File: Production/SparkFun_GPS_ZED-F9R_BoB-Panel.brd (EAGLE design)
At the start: 43.2 x 50.8 mm, 140 parts, among them J1 U.FL, J3 QWIIC_RIGHT_ANGLE, J4 QWIIC_RIGHT_ANGLE, U1 DUAL-OPTO_HCPL-073L, U2 U-BLOX_ZED_F9R, U3 UHS_INVERTER_SCHMITT_TRIGGERS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, U4 UHS_INVERTER_SCHMITT_TRIGGERS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, U5 3.3V

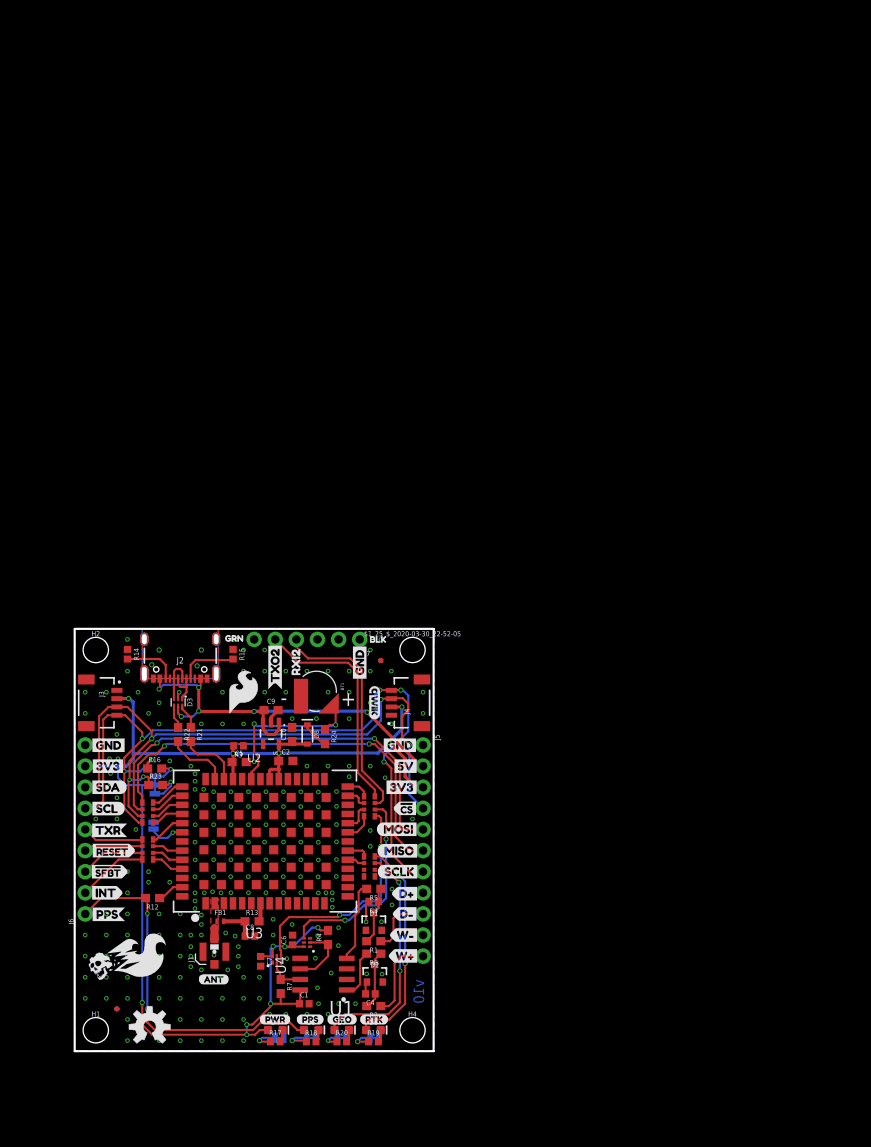
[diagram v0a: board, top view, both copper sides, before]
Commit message: Adds panel to files, deletes buzzard labels
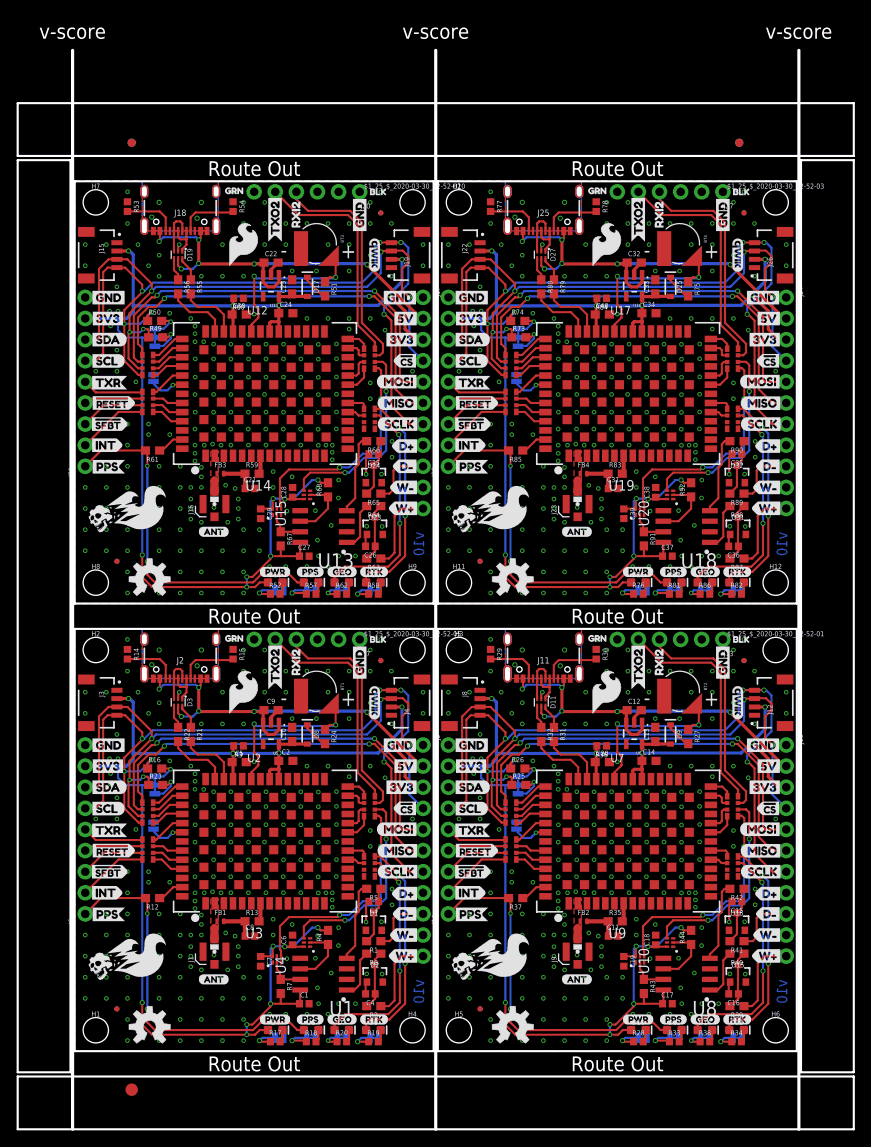
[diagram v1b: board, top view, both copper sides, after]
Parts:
- removed FRAME1: FRAME-LEDGER, SparkFun-Aesthetics:CREATIVE_COMMONS
- added $1_25_$_2020-03-30_22-52-01, $1_25_$_2020-03-30_22-52-02, $1_25_$_2020-03-30_22-52-03, H10, H11, H12, H3, H5, H6, H7, H8, H9: STAND-OFFTIGHT, SparkFun-Hardware:STAND-OFF-TIGHT
- added BT2, BT3, BT4: ML414H_IV01E_BATTERY, SparkFun-Batteries:ML414H_IV01E
- added C11, C21, C31: 47pF, SparkFun-Capacitors:0402
- added C12, C13, C14, C20, C22, C23, C24, C30, C32, C33, C34, C40: 1.0uF, SparkFun-Capacitors:0603
- added C15, C16, C25, C26, C35, C36: 1nF, SparkFun-Capacitors:0402
- added C17, C18, C19, C27, C28, C29, C37, C38, C39: 0.1uF, SparkFun-Capacitors:0402
- added D10, D18, D26: RED, SparkFun-LED:LED-0603
- added D11, D19, D27: PRTR5V0U2F, SparkFun-IC-Power:SOT886
- added D12, D13, D14, D20, D21, D22, D28, D29, D30: BLUE, SparkFun-LED:LED-0603
- added D15, D16, D23, D24, D31, D32: 15V, SparkFun-DiscreteSemi:SOT23-3
- added D17, D25, D9: 0.5A/40V/420mV, SparkFun-DiscreteSemi:SOD-323
- added E$1, E$2, E$3, E$4: (no value), SparkFun-Aesthetics:FIDUCIAL-1X2
- added E$5: (no value), SparkFun-Retired:FIDUCIAL-1.5X3
- added FB2, FB3, FB4: 120NH, SparkFun-Coils:0402_MURATA
- added FD10, FD11, FD12, FD13, FD14, FD15, FD16, FD5, FD6, FD7, FD8, FD9: FIDUCIALUFIDUCIAL, SparkFun-Aesthetics:FIDUCIAL-MICRO
- added J10, J17, J24: (no value), SparkFun-Connectors:1X11_NO_SILK
- added J11, J18, J25: (no value), SparkFun-Connectors:USB-C-16P-2LAYER-PADS
- added J12, J15, J19, J22, J26, J8: QWIIC_RIGHT_ANGLE, SparkFun-Connectors:JST04_1MM_RA
- added J13, J20, J27: (no value), SparkFun-Connectors:1X06_NO_SILK
- added J14, J21, J28: (no value), SparkFun-Connectors:1X09_NO_SILK
- added J16, J23, J9: U.FL, SparkFun-Connectors:U.FL
- added JP10, JP11, JP12, JP15, JP16, JP17, JP18, JP21, JP22, JP23, JP24, JP9: JUMPER-SMT_2_NC_TRACE_SILK, SparkFun-Jumpers:SMT-JUMPER_2_NC_TRACE_SILK
- added JP13, JP19, JP7: JUMPER-SMT_3_2-NC_TRACE_SILK, SparkFun-Jumpers:SMT-JUMPER_3_2-NC_TRACE_SILK
- added JP14, JP20, JP8: JUMPER-SMT_2_NO_SILK, SparkFun-Jumpers:SMT-JUMPER_2_NO_SILK
- added LOGO10, LOGO4, LOGO7: SFE_LOGO_NAME_FLAME.2_INCH, SparkFun-Aesthetics:SFE_LOGO_NAME_FLAME_.2
- added LOGO11, LOGO5, LOGO8: QWIIC_LOGO_4MM, SparkFun-Aesthetics:QWIIC_4MM
- added LOGO12, LOGO6, LOGO9: OSHW-LOGOM, SparkFun-Aesthetics:OSHW-LOGO-M
- added R25, R26, R49, R50, R73, R74: 2.2k, SparkFun-Resistors:0603
- added R27, R39, R41, R51, R63, R65, R75, R87, R89: 3.3k, SparkFun-Resistors:0603
- added R28, R33, R34, R38, R52, R57, R58, R62, R76, R81, R82, R86: 1KOHM-0402-1/16W-1%, SparkFun-Resistors:0402
- added R29, R30, R53, R54, R77, R78: 5.1k, SparkFun-Resistors:0402
- added R31, R32, R55, R56, R79, R80: 27, SparkFun-Resistors:0603
- added R35, R37, R59, R61, R83, R85: 33, SparkFun-Resistors:0603
- added R36, R60, R84: 100K, SparkFun-Resistors:0402
- added R40, R42, R64, R66, R88, R90: 470, SparkFun-Resistors:0603
- added R43, R44, R67, R68, R91, R92: 910, SparkFun-Resistors:0603
- added R45, R46, R47, R48, R69, R70, R71, R72, R93, R94, R95, R96: 33, SparkFun-Resistors:1206_RA
- added U$100, U$166, U$232: (no value), corrected_safe_reset:#RESET2
- added U$101, U$167, U$233: (no value), corrected_safe_reset:#SAFEBOOT3
- added U$102, U$168, U$234: (no value), wat-for-reals:#SFBT0
- added U$103, U$104, U$169, U$170, U$235, U$236: (no value), wat-for-reals:GEO1
- added U$105, U$118, U$171, U$184, U$237, U$250: (no value), wt_dir:D#0
- added U$106, U$119, U$172, U$185, U$238, U$251: (no value), wt_dir:D#1
- added U$107, U$120, U$173, U$186, U$239, U$252: (no value), wt_dir:W#2
- added U$108, U$121, U$174, U$187, U$240, U$253: (no value), wt_dir:W#3
- added U$109, U$175, U$241: (no value), SparkFun-Aesthetics:SFE_LOGO_FLAME_.2
- added U$110, U$176, U$242: (no value), Labels:SCL-[)
- added U$111, U$177, U$243: (no value), Labels:SDA-[)
- added U$112, U$114, U$139, U$141, U$178, U$180, U$205, U$207, U$244, U$246, U$73, U$75: (no value), Labels:3V3-04
- added U$113, U$115, U$125, U$140, U$142, U$144, U$179, U$181, U$191, U$206, U$208, U$210, U$245, U$247, U$257, U$74, U$76, U$78: (no value), Labels:GND-04
- added U$116, U$182, U$248: (no value), Labels:MISO-(]-04
- added U$117, U$183, U$249: (no value), Labels:MOSI-(]-04
- added U$122, U$143, U$188, U$209, U$254, U$77: (no value), Labels:5V
- added U$123, U$189, U$255: (no value), ALL_LABELS:INT1
- added U$124, U$190, U$256: (no value), ALL_LABELS:PPS4
- added U$126, U$146, U$192, U$212, U$258, U$80: (no value), moar:TXO21
- added U$127, U$193, U$259: (no value), txr_rxi:RXI22
- added U$128, U$194, U$260: (no value), txr_rxi:SCLK1
- added U$129, U$195, U$261: (no value), txr_rxi:TXR0
- added U$130, U$196, U$262: (no value), dead reckoning:GPS_DEAD_RECKONING0
- added U$131, U$197, U$263: (no value), Dead#Reckoning#GPS#board#silk#FINAL#png:DEAD#RECKONING#GPS#BOARD#SILK#FINAL#JPG
- added U$132, U$198, U$264: (no value), Dead#Reckoning#GPS#board#silk#FINALSMALL:DEAD#RECKONING#GPS#BOARD#SILK#FINAL#JPG
- added U$133, U$199, U$32: (no value), Labels:CS#-<]-04
- added U$134, U$150, U$200, U$216, U$50, U$84: (no value), ALL labels:PPS8
- added U$135, U$151, U$201, U$217, U$52, U$85: (no value), ALL labels:PWR10
- added U$136, U$149, U$202, U$215, U$57, U$83: (no value), ALL labels:RTK9
- added U$137, U$155, U$203, U$221, U$63, U$89: (no value), TXR:BLK2
- added U$138, U$154, U$204, U$220, U$72, U$88: (no value), TXR:GRN1
- added U$145, U$211, U$79: (no value), ALL_LABELS:RXI28
- added U$147, U$213, U$81: (no value), more_all_labels:SPI4
- added U$148, U$214, U$82: (no value), Labels:I_SUPER2_C-()-04
- added U$152, U$218, U$86: (no value), ant:ANT0
- added U$153, U$219, U$87: (no value), zed:ZED#F9R0
- added U$156, U$222, U$90: (no value), bottom labels:INT2
- added U$157, U$223, U$91: (no value), bottom labels:PPS1
- added U$158, U$224, U$92: (no value), Labels:CS#-[>-04
- added U$159, U$225, U$93: (no value), corrected_bottom:RXI#MOSI0
- added U$160, U$226, U$94: (no value), corrected_bottom:TXO#MISO1
- added U$161, U$227, U$95: (no value), corrected_bottom:SCL#CLK2
- added U$162, U$228, U$96: (no value), corrected_bottom:SCL5
- added U$163, U$229, U$97: (no value), corrected_bottom:SDA4
- added U$164, U$230, U$98: (no value), corrected_bottom:TXR3
- added U$165, U$231, U$99: (no value), corrected_safe_reset:#RESET1
- added U10, U14, U15, U19, U20, U9: UHS_INVERTER_SCHMITT_TRIGGERSIP6, SparkFun-IC-Amplifiers:SIP6
- added U11, U16, U6: 3.3V, SparkFun-IC-Power:SOT23-5
- added U12, U17, U7: U-BLOX_ZED_F9R, SparkFun-GPS:UBLOX_ZED_F9R
- added U13, U18, U8: DUAL-OPTO_HCPL-073L, SparkFun-DiscreteSemi:SOP_8-PIN
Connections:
- new net !RESET1: J14.4, R46.P2
- new net !RESET2: J21.4, R70.P2
- new net !RESET3: J28.4, R94.P2
- new net !SAFEBOOT1: J14.3, R46.P3
- new net !SAFEBOOT2: J21.3, R70.P3
- new net !SAFEBOOT3: J28.3, R94.P3
- new net 3.3V1: C13.1, C14.1, C17.1, C18.1, C19.1, C20.1, D10.A, D9.A, J10.3, J12.2, J14.8, J8.2, JP7.2, R36.2, R43.2, R44.2, U10.P6, U6.5, U7.P33, U7.P34, U7.P38, U8.P8, U9.P6
- new net 3.3V2: C23.1, C24.1, C27.1, C28.1, C29.1, C30.1, D17.A, D18.A, J15.2, J17.3, J19.2, J21.8, JP13.2, R60.2, R67.2, R68.2, U11.5, U12.P33, U12.P34, U12.P38, U13.P8, U14.P6, U15.P6
- new net 3.3V3: C33.1, C34.1, C37.1, C38.1, C39.1, C40.1, D25.A, D26.A, J22.2, J24.3, J26.2, J28.8, JP19.2, R84.2, R91.2, R92.2, U16.5, U17.P33, U17.P34, U17.P38, U18.P8, U19.P6, U20.P6
- new net DIR+1: J10.9, R41.1
- new net DIR+2: J17.9, R65.1
- new net DIR+3: J24.9, R89.1
- new net DIR_IN1: R42.2, U8.P4
- new net DIR_IN2: R66.2, U13.P4
- new net DIR_IN3: R90.2, U18.P4
- new net DIR_OUT1: R47.P6, U10.P4
- new net DIR_OUT2: R71.P6, U15.P4
- new net DIR_OUT3: R95.P6, U20.P4
- new net DIR_SCHMITT1: R44.1, U10.P2, U8.P6
- new net DIR_SCHMITT2: R68.1, U13.P6, U15.P2
- new net DIR_SCHMITT3: R92.1, U18.P6, U20.P2
- new net DMINUS1: R31.2, U7.P39
- new net DMINUS2: R55.2, U12.P39
- new net DMINUS3: R79.2, U17.P39
- new net DPLUS1: R32.2, U7.P40
- new net DPLUS2: R56.2, U12.P40
- new net DPLUS3: R80.2, U17.P40
- new net D_SEL1: JP8.1, U7.P47
- new net D_SEL2: JP14.1, U12.P47
- new net D_SEL3: JP20.1, U17.P47
- new net GEOF_STAT1: D14.A, R48.P7
- new net GEOF_STAT2: D22.A, R72.P7
- new net GEOF_STAT3: D30.A, R96.P7
- new net GND1: BT2.-, C11.2, C12.2, C13.2, C14.2, C15.2, C16.2, C17.2, C18.2, C19.2, C20.2, D11.2, D15.1, D16.1, J10.1, J10.10, J10.8, J11.GND, J11.GND2, J12.1, J13.1, J14.9, J8.1, J9.1, J9.2, JP10.1, JP11.1, JP12.1, JP8.2, JP9.1, R29.1, R30.1, R36.1, U10.P3, U6.2, U7.G1, U7.G10, U7.G11, U7.G12, U7.G13, U7.G14, U7.G15, U7.G16, U7.G17, U7.G18, U7.G19, U7.G2, U7.G20, U7.G21, U7.G22, U7.G23, U7.G24, U7.G25, U7.G26, U7.G27, U7.G28, U7.G29, U7.G3, U7.G30, U7.G31, U7.G32, U7.G33, U7.G34, U7.G35, U7.G36, U7.G37, U7.G38, U7.G39, U7.G4, U7.G40, U7.G41, U7.G42, U7.G43, U7.G44, U7.G45, U7.G46, U7.G47, U7.G48, U7.G5, U7.G6, U7.G7, U7.G8, U7.G9, U7.P1, U7.P12, U7.P14, U7.P3, U7.P32, U7.P37, U7.P41, U7.P48, U8.P2, U8.P3, U8.P5, U9.P3
- new net GND2: BT3.-, C21.2, C22.2, C23.2, C24.2, C25.2, C26.2, C27.2, C28.2, C29.2, C30.2, D19.2, D23.1, D24.1, J15.1, J16.1, J16.2, J17.1, J17.10, J17.8, J18.GND, J18.GND2, J19.1, J20.1, J21.9, JP14.2, JP15.1, JP16.1, JP17.1, JP18.1, R53.1, R54.1, R60.1, U11.2, U12.G1, U12.G10, U12.G11, U12.G12, U12.G13, U12.G14, U12.G15, U12.G16, U12.G17, U12.G18, U12.G19, U12.G2, U12.G20, U12.G21, U12.G22, U12.G23, U12.G24, U12.G25, U12.G26, U12.G27, U12.G28, U12.G29, U12.G3, U12.G30, U12.G31, U12.G32, U12.G33, U12.G34, U12.G35, U12.G36, U12.G37, U12.G38, U12.G39, U12.G4, U12.G40, U12.G41, U12.G42, U12.G43, U12.G44, U12.G45, U12.G46, U12.G47, U12.G48, U12.G5, U12.G6, U12.G7, U12.G8, U12.G9, U12.P1, U12.P12, U12.P14, U12.P3, U12.P32, U12.P37, U12.P41, U12.P48, U13.P2, U13.P3, U13.P5, U14.P3, U15.P3
- new net GND3: BT4.-, C31.2, C32.2, C33.2, C34.2, C35.2, C36.2, C37.2, C38.2, C39.2, C40.2, D27.2, D31.1, D32.1, J22.1, J23.1, J23.2, J24.1, J24.10, J24.8, J25.GND, J25.GND2, J26.1, J27.1, J28.9, JP20.2, JP21.1, JP22.1, JP23.1, JP24.1, R77.1, R78.1, R84.1, U16.2, U17.G1, U17.G10, U17.G11, U17.G12, U17.G13, U17.G14, U17.G15, U17.G16, U17.G17, U17.G18, U17.G19, U17.G2, U17.G20, U17.G21, U17.G22, U17.G23, U17.G24, U17.G25, U17.G26, U17.G27, U17.G28, U17.G29, U17.G3, U17.G30, U17.G31, U17.G32, U17.G33, U17.G34, U17.G35, U17.G36, U17.G37, U17.G38, U17.G39, U17.G4, U17.G40, U17.G41, U17.G42, U17.G43, U17.G44, U17.G45, U17.G46, U17.G47, U17.G48, U17.G5, U17.G6, U17.G7, U17.G8, U17.G9, U17.P1, U17.P12, U17.P14, U17.P3, U17.P32, U17.P37, U17.P41, U17.P48, U18.P2, U18.P3, U18.P5, U19.P3, U20.P3
- new net INT1: J14.2, R46.P4
- new net INT2: J21.2, R70.P4
- new net INT3: J28.2, R94.P4
- new net N$100: R71.P4, U12.P22
- new net N$101: R71.P3, U12.P23
- new net N$102: JP18.2, R62.1
- new net N$103: D22.C, R62.2
- new net N$104: C26.1, D23.3, R63.2, R64.1
- new net N$105: C25.1, D24.3, R65.2, R66.1
- new net N$106: D25.C, R75.2
- new net N$107: JP19.1, R73.2
- new net N$108: JP19.3, R74.2
- new net N$109: J25.B5, R77.2
- new net N$110: J25.A5, R78.2
- new net N$111: JP22.2, R82.1
- new net N$112: JP23.2, R81.1
- new net N$113: D28.C, R81.2
- new net N$114: D29.C, R82.2
- new net N$115: D26.C, R76.2
- new net N$116: JP21.2, R76.1
- new net N$117: C31.1, FB4.P2, R83.1
- new net N$118: D27.3, J25.A6, J25.B6
- new net N$119: D27.1, J25.A7, J25.B7
- new net N$120: D27.6, R79.1
- new net N$121: D27.4, R80.1
- new net N$122: R94.P7, U17.P49
- new net N$123: R94.P5, U17.P51
- new net N$124: R93.P6, U17.P44
- new net N$125: R93.P5, U17.P45
- new net N$126: R94.P8, U17.P46
- new net N$127: R93.P8, U17.P42
- new net N$128: R93.P7, U17.P43
- new net N$129: R95.P1, U17.P27
- new net N$13: D9.C, R27.2
- new net N$130: R95.P2, U17.P26
- new net N$131: R96.P2, U17.P19
- new net N$132: R96.P1, U17.P20
- new net N$133: R85.1, U17.P53
- new net N$134: R94.P6, U17.P50
- new net N$135: R95.P4, U17.P22
- new net N$136: R95.P3, U17.P23
- new net N$137: JP24.2, R86.1
- new net N$138: D30.C, R86.2
- new net N$139: C36.1, D31.3, R87.2, R88.1
- new net N$140: C35.1, D32.3, R89.2, R90.1
- new net N$36: JP7.1, R25.2
- new net N$38: JP7.3, R26.2
- new net N$39: J11.B5, R29.2
- new net N$40: J11.A5, R30.2
- new net N$41: JP10.2, R34.1
- new net N$42: JP11.2, R33.1
- new net N$43: D12.C, R33.2
- new net N$44: D13.C, R34.2
- new net N$45: D10.C, R28.2
- new net N$46: JP9.2, R28.1
- new net N$47: C11.1, FB2.P2, R35.1
- new net N$48: D11.3, J11.A6, J11.B6
- new net N$49: D11.1, J11.A7, J11.B7
- new net N$50: D11.6, R31.1
- new net N$51: D11.4, R32.1
- new net N$52: R46.P7, U7.P49
- new net N$53: R46.P5, U7.P51
- new net N$54: R45.P6, U7.P44
- new net N$55: R45.P5, U7.P45
- new net N$56: R46.P8, U7.P46
- new net N$57: R45.P8, U7.P42
- new net N$58: R45.P7, U7.P43
- new net N$59: R47.P1, U7.P27
- new net N$60: R47.P2, U7.P26
- new net N$61: R48.P2, U7.P19
- new net N$62: R48.P1, U7.P20
- new net N$63: R37.1, U7.P53
- new net N$64: R46.P6, U7.P50
- new net N$65: R47.P4, U7.P22
- new net N$66: R47.P3, U7.P23
- new net N$67: JP12.2, R38.1
- new net N$68: D14.C, R38.2
- new net N$69: C16.1, D15.3, R39.2, R40.1
- new net N$70: C15.1, D16.3, R41.2, R42.1
- new net N$71: D17.C, R51.2
- new net N$72: JP13.1, R49.2
- new net N$73: JP13.3, R50.2
- new net N$74: J18.B5, R53.2
- new net N$75: J18.A5, R54.2
- new net N$76: JP16.2, R58.1
- new net N$77: JP17.2, R57.1
- new net N$78: D20.C, R57.2
- new net N$79: D21.C, R58.2
- new net N$80: D18.C, R52.2
- new net N$81: JP15.2, R52.1
- new net N$82: C21.1, FB3.P2, R59.1
- new net N$83: D19.3, J18.A6, J18.B6
- new net N$84: D19.1, J18.A7, J18.B7
- new net N$85: D19.6, R55.1
- new net N$86: D19.4, R56.1
- new net N$87: R70.P7, U12.P49
- new net N$88: R70.P5, U12.P51
- new net N$89: R69.P6, U12.P44
- new net N$90: R69.P5, U12.P45
- new net N$91: R70.P8, U12.P46
- new net N$92: R69.P8, U12.P42
- new net N$93: R69.P7, U12.P43
- new net N$94: R71.P1, U12.P27
- new net N$95: R71.P2, U12.P26
- new net N$96: R72.P2, U12.P19
- new net N$97: R72.P1, U12.P20
- new net N$98: R61.1, U12.P53
- new net N$99: R70.P6, U12.P50
- new net PPS1: D12.A, J14.1, R37.2
- new net PPS2: D20.A, J21.1, R61.2
- new net PPS3: D28.A, J28.1, R85.2
- new net RF_IN1: FB2.P1, J9.FEED, U7.P2
- new net RF_IN2: FB3.P1, J16.FEED, U12.P2
- new net RF_IN3: FB4.P1, J23.FEED, U17.P2
- new net RTK_STAT1: D13.A, R48.P8
- new net RTK_STAT2: D21.A, R72.P8
- new net RTK_STAT3: D29.A, R96.P8
- new net RXI/MOSI1: J10.5, R45.P2
- new net RXI/MOSI2: J17.5, R69.P2
- new net RXI/MOSI3: J24.5, R93.P2
- new net RXI1: J13.4, R47.P7
- new net RXI3: J20.4, R71.P7
- new net RXI4: J27.4, R95.P7
- new net SCL/CLK1: J10.7, J12.4, J14.6, J8.4, R26.1, R45.P4
- new net SCL/CLK2: J15.4, J17.7, J19.4, J21.6, R50.1, R69.P4
- new net SCL/CLK3: J22.4, J24.7, J26.4, J28.6, R74.1, R93.P4
- new net SDA/!CS1: J10.4, J12.3, J14.7, J8.3, R25.1, R45.P3
- new net SDA/!CS2: J15.3, J17.4, J19.3, J21.7, R49.1, R69.P3
- new net SDA/!CS3: J22.3, J24.4, J26.3, J28.7, R73.1, R93.P3
- new net SHIELD1: J11.SHLD1, J11.SHLD2, J11.SHLD3, J11.SHLD4
- new net SHIELD2: J18.SHLD1, J18.SHLD2, J18.SHLD3, J18.SHLD4
- new net SHIELD3: J25.SHLD1, J25.SHLD2, J25.SHLD3, J25.SHLD4
- new net TXO/MISO1: J10.6, R45.P1
- new net TXO/MISO2: J17.6, R69.P1
- new net TXO/MISO3: J24.6, R93.P1
- new net TXO1: J13.5, R47.P8
- new net TXO3: J20.5, R71.P8
- new net TXO4: J27.5, R95.P8
- new net TX_READY1: J14.5, R46.P1
- new net TX_READY2: J21.5, R70.P1
- new net TX_READY3: J28.5, R94.P1
- new net VIN1: C12.1, D11.5, J10.2, J11.VBUS1, J11.VBUS2, U6.1, U6.3
- new net VIN2: C22.1, D19.5, J17.2, J18.VBUS1, J18.VBUS2, U11.1, U11.3
- new net VIN3: C32.1, D27.5, J24.2, J25.VBUS1, J25.VBUS2, U16.1, U16.3
- new net V_BATT1: BT2.+, R27.1, U7.P36
- new net V_BATT2: BT3.+, R51.1, U12.P36
- new net V_BATT3: BT4.+, R75.1, U17.P36
- new net V_RF1: R35.2, U7.P7
- new net V_RF2: R59.2, U12.P7
- new net V_RF3: R83.2, U17.P7
- new net WT+1: J10.11, R39.1
- new net WT+2: J17.11, R63.1
- new net WT+3: J24.11, R87.1
- new net WT_IN1: R40.2, U8.P1
- new net WT_IN2: R64.2, U13.P1
- new net WT_IN3: R88.2, U18.P1
- new net WT_OUT1: R47.P5, U9.P4
- new net WT_OUT2: R71.P5, U14.P4
- new net WT_OUT3: R95.P5, U19.P4
- new net WT_SCHMITT1: R43.1, U8.P7, U9.P2
- new net WT_SCHMITT2: R67.1, U13.P7, U14.P2
- new net WT_SCHMITT3: R91.1, U18.P7, U19.P2
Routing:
- net 3.3V3: track 0.00 -> 157.0 mm, vias 0 -> 12
- net 3.3V2: track 0.00 -> 157.0 mm, vias 0 -> 12
- net 3.3V1: track 0.00 -> 157.0 mm, vias 0 -> 12
- net SCL/CLK3: track 0.00 -> 97.9 mm, vias 0 -> 6
- net SCL/CLK2: track 0.00 -> 97.9 mm, vias 0 -> 6
- net SCL/CLK1: track 0.00 -> 97.9 mm, vias 0 -> 6
- net SDA/!CS2: track 0.00 -> 82.3 mm, vias 0 -> 5
- net SDA/!CS1: track 0.00 -> 82.3 mm, vias 0 -> 5
- net SDA/!CS3: track 0.00 -> 82.3 mm, vias 0 -> 5
- net RXI/MOSI1: track 0.00 -> 51.3 mm, vias 0 -> 2
- net RXI/MOSI3: track 0.00 -> 51.3 mm, vias 0 -> 2
- net RXI/MOSI2: track 0.00 -> 51.3 mm, vias 0 -> 2
- net VIN3: track 0.00 -> 50.7 mm, vias 0 -> 6
- net VIN2: track 0.00 -> 50.7 mm, vias 0 -> 6
- net VIN1: track 0.00 -> 50.7 mm, vias 0 -> 6
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- added copper zone on layer 1, net GND1
- added copper zone on layer 16, net GND1
- added copper zone on layer 1, net GND2
- added copper zone on layer 16, net GND2
- added copper zone on layer 1, net GND3
- added copper zone on layer 16, net GND3
- added copper zone on layer 1, net RF_IN1
- added copper zone on layer 1, net RF_IN2
- added copper zone on layer 1, net RF_IN3
- added copper zone on layer 1, net SHIELD1
- added copper zone on layer 16, net SHIELD1
- added copper zone on layer 1, net SHIELD2
- added copper zone on layer 16, net SHIELD2
- added copper zone on layer 1, net SHIELD3
- added copper zone on layer 16, net SHIELD3
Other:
- board size 43.2 x 50.8 mm -> 100.6 x 129.8 mm
- board text added: "Route Out"
- board text added: "v-score"
- board text removed: "Elias Santistevan"
- board text removed: "Units In Inches"

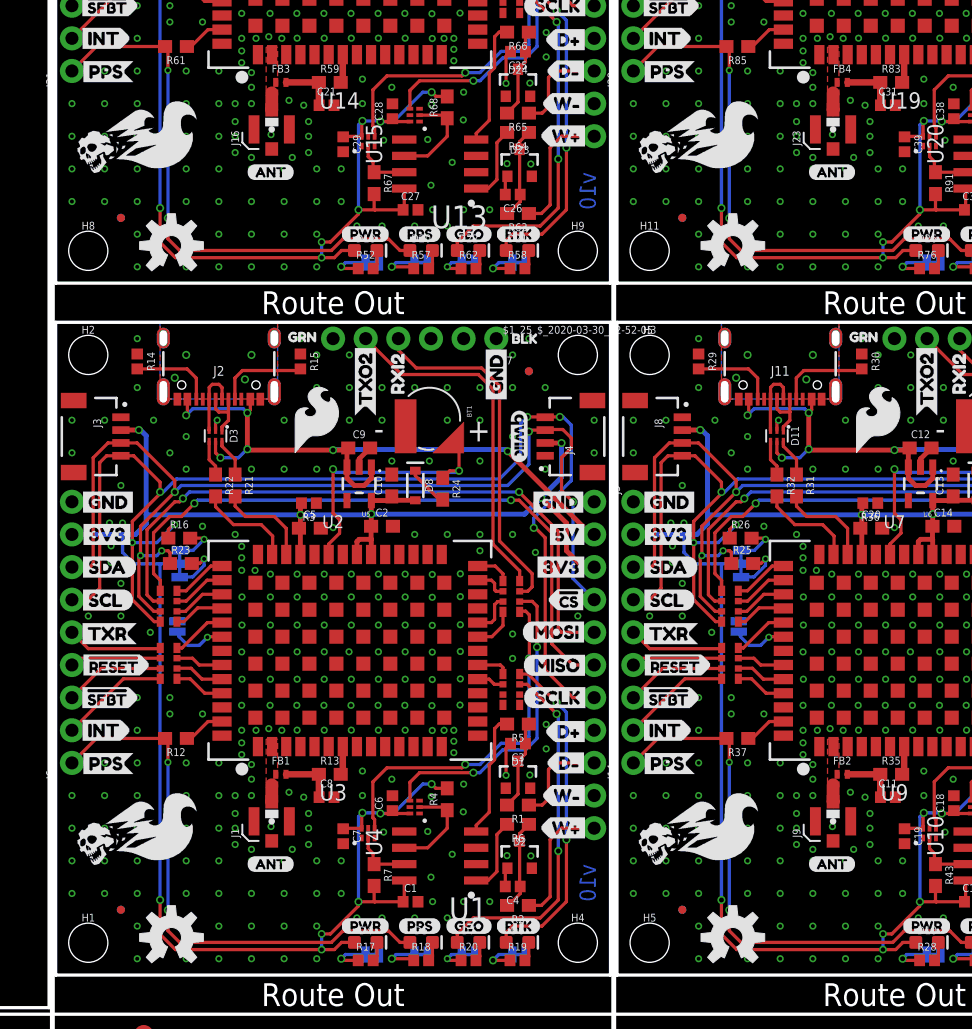
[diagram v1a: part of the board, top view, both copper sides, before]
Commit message: Adds silk for 3 axes and repanelizes
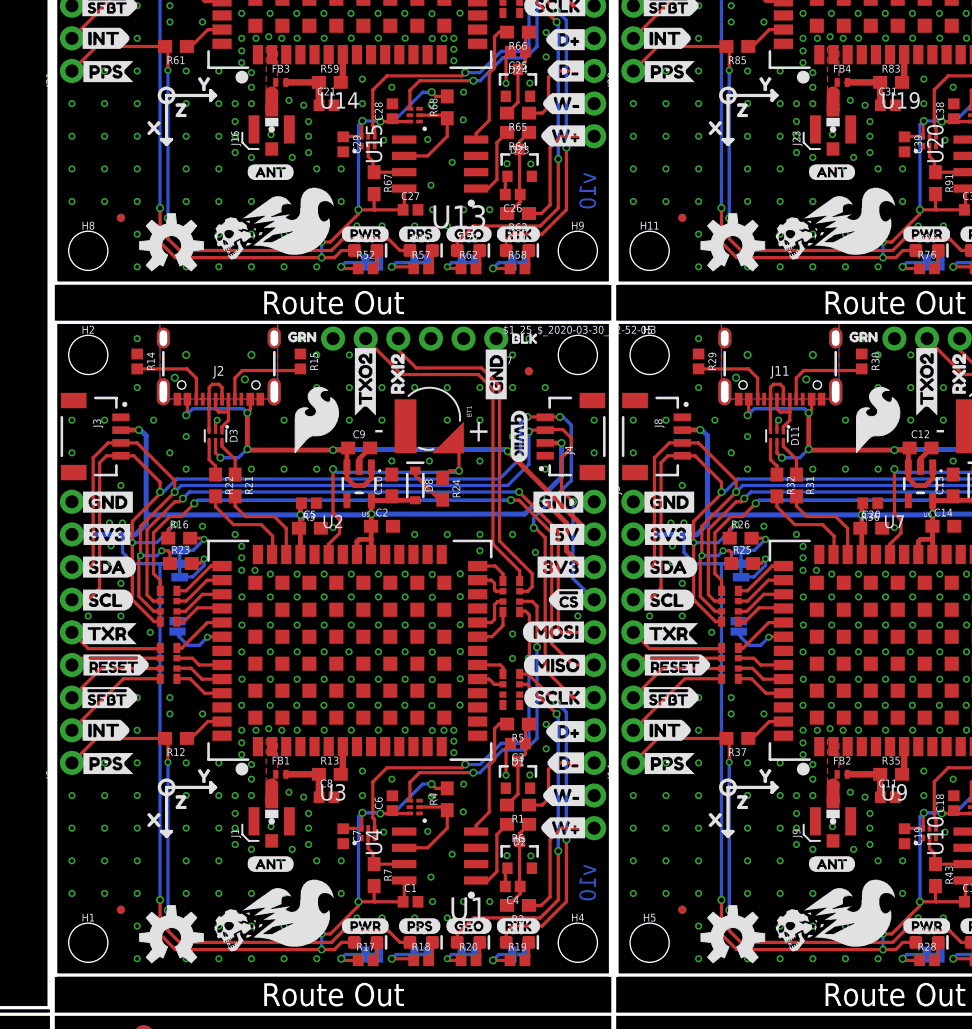
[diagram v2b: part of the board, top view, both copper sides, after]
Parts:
- added U$265: (no value), wt_dir:D#0
- added U$266: (no value), wt_dir:D#1
- added U$267: (no value), wt_dir:W#2
- added U$268: (no value), wt_dir:W#3
- added U$269: (no value), Labels:5V
- added U$270: (no value), ALL_LABELS:INT1
- added U$271: (no value), ALL_LABELS:PPS4
- added U$272: (no value), Labels:GND-04
- added U$273: (no value), moar:TXO21
- added U$274: (no value), txr_rxi:RXI22
- added U$275: (no value), txr_rxi:SCLK1
- added U$276: (no value), txr_rxi:TXR0
- added U$277: (no value), dead reckoning:GPS_DEAD_RECKONING0
- added U$278: (no value), Dead#Reckoning#GPS#board#silk#FINAL#png:DEAD#RECKONING#GPS#BOARD#SILK#FINAL#JPG
- added U$279: (no value), Dead#Reckoning#GPS#board#silk#FINALSMALL:DEAD#RECKONING#GPS#BOARD#SILK#FINAL#JPG
- added U$280: (no value), Orientation:X1
- added U$281, U$282: (no value), Orientation:Y2
- added U$283, U$284: (no value), Orientation:Z0
- U$100: device corrected_safe_reset:#RESET2 -> corrected_bottom:SCL#CLK2
- U$101: device corrected_safe_reset:#SAFEBOOT3 -> corrected_bottom:SCL5
- U$102: device wat-for-reals:#SFBT0 -> corrected_bottom:SDA4
- U$103: device wat-for-reals:GEO1 -> corrected_bottom:TXR3
- U$104: device wat-for-reals:GEO1 -> corrected_safe_reset:#RESET1
- U$105: device wt_dir:D#0 -> corrected_safe_reset:#RESET2
- U$106: device wt_dir:D#1 -> corrected_safe_reset:#SAFEBOOT3
- U$107: device wt_dir:W#2 -> wat-for-reals:#SFBT0
- U$108: device wt_dir:W#3 -> wat-for-reals:GEO1
- U$109: device SparkFun-Aesthetics:SFE_LOGO_FLAME_.2 -> wat-for-reals:GEO1
- U$110: device Labels:SCL-[) -> wt_dir:D#0
- U$111: device Labels:SDA-[) -> wt_dir:D#1
- U$112: device Labels:3V3-04 -> wt_dir:W#2
- U$113: device Labels:GND-04 -> wt_dir:W#3
- U$114: device Labels:3V3-04 -> SparkFun-Aesthetics:SFE_LOGO_FLAME_.2
- U$115, U$257: device Labels:GND-04 -> Labels:SCL-[)
- U$116: device Labels:MISO-(]-04 -> Labels:SDA-[)
- U$117: device Labels:MOSI-(]-04 -> Labels:3V3-04
- U$118: device wt_dir:D#0 -> Labels:GND-04
- U$119: device wt_dir:D#1 -> Labels:3V3-04
- U$120: device wt_dir:W#2 -> Labels:GND-04
- U$121: device wt_dir:W#3 -> Labels:MISO-(]-04
- U$122: device Labels:5V -> Labels:MOSI-(]-04
- U$123: device ALL_LABELS:INT1 -> wt_dir:D#0
- U$124: device ALL_LABELS:PPS4 -> wt_dir:D#1
- U$125: device Labels:GND-04 -> wt_dir:W#2
- U$126: device moar:TXO21 -> wt_dir:W#3
- U$127: device txr_rxi:RXI22 -> Labels:5V
- U$128: device txr_rxi:SCLK1 -> ALL_LABELS:INT1
- U$129: device txr_rxi:TXR0 -> ALL_LABELS:PPS4
- U$130, U$262: device dead reckoning:GPS_DEAD_RECKONING0 -> Labels:GND-04
- U$131: device Dead#Reckoning#GPS#board#silk#FINAL#png:DEAD#RECKONING#GPS#BOARD#SILK#FINAL#JPG -> moar:TXO21
- U$132: device Dead#Reckoning#GPS#board#silk#FINALSMALL:DEAD#RECKONING#GPS#BOARD#SILK#FINAL#JPG -> txr_rxi:RXI22
- U$133: device Labels:CS#-<]-04 -> txr_rxi:SCLK1
- U$134: device ALL labels:PPS8 -> txr_rxi:TXR0
- U$135: device ALL labels:PWR10 -> dead reckoning:GPS_DEAD_RECKONING0
- U$136: device ALL labels:RTK9 -> Dead#Reckoning#GPS#board#silk#FINAL#png:DEAD#RECKONING#GPS#BOARD#SILK#FINAL#JPG
- U$137: device TXR:BLK2 -> Dead#Reckoning#GPS#board#silk#FINALSMALL:DEAD#RECKONING#GPS#BOARD#SILK#FINAL#JPG
- U$138: device TXR:GRN1 -> Orientation:X1
- U$139: device Labels:3V3-04 -> Orientation:Y2
- U$140, U$210: device Labels:GND-04 -> Orientation:Y2
- U$141: device Labels:3V3-04 -> Orientation:Z0
- U$142: device Labels:GND-04 -> Orientation:Z0
- U$143: device Labels:5V -> Labels:CS#-<]-04
- U$144: device Labels:GND-04 -> ALL labels:PPS8
- U$145: device ALL_LABELS:RXI28 -> ALL labels:PWR10
- U$146: device moar:TXO21 -> ALL labels:RTK9
- U$147: device more_all_labels:SPI4 -> TXR:BLK2
- U$148: device Labels:I_SUPER2_C-()-04 -> TXR:GRN1
- U$149: device ALL labels:RTK9 -> Labels:3V3-04
- U$150: device ALL labels:PPS8 -> Labels:GND-04
- U$151: device ALL labels:PWR10 -> Labels:3V3-04
- U$152: device ant:ANT0 -> Labels:GND-04
- U$153: device zed:ZED#F9R0 -> Labels:5V
- U$154: device TXR:GRN1 -> Labels:GND-04
- U$155: device TXR:BLK2 -> ALL_LABELS:RXI28
- U$156: device bottom labels:INT2 -> moar:TXO21
- U$157: device bottom labels:PPS1 -> more_all_labels:SPI4
- U$158: device Labels:CS#-[>-04 -> Labels:I_SUPER2_C-()-04
- U$159: device corrected_bottom:RXI#MOSI0 -> ALL labels:RTK9
- U$160: device corrected_bottom:TXO#MISO1 -> ALL labels:PPS8
- U$161: device corrected_bottom:SCL#CLK2 -> ALL labels:PWR10
- U$162: device corrected_bottom:SCL5 -> ant:ANT0
- U$163: device corrected_bottom:SDA4 -> zed:ZED#F9R0
- U$164: device corrected_bottom:TXR3 -> TXR:GRN1
- U$165: device corrected_safe_reset:#RESET1 -> TXR:BLK2
- U$166: device corrected_safe_reset:#RESET2 -> bottom labels:INT2
- U$167: device corrected_safe_reset:#SAFEBOOT3 -> bottom labels:PPS1
- U$168: device wat-for-reals:#SFBT0 -> Labels:CS#-[>-04
- U$169: device wat-for-reals:GEO1 -> corrected_bottom:RXI#MOSI0
- U$170: device wat-for-reals:GEO1 -> corrected_bottom:TXO#MISO1
- U$171: device wt_dir:D#0 -> corrected_bottom:SCL#CLK2
- U$172: device wt_dir:D#1 -> corrected_bottom:SCL5
- U$173: device wt_dir:W#2 -> corrected_bottom:SDA4
- U$174: device wt_dir:W#3 -> corrected_bottom:TXR3
- U$175: device SparkFun-Aesthetics:SFE_LOGO_FLAME_.2 -> corrected_safe_reset:#RESET1
- U$176: device Labels:SCL-[) -> corrected_safe_reset:#RESET2
- U$177: device Labels:SDA-[) -> corrected_safe_reset:#SAFEBOOT3
- U$178: device Labels:3V3-04 -> wat-for-reals:#SFBT0
- U$179: device Labels:GND-04 -> wat-for-reals:GEO1
- U$180: device Labels:3V3-04 -> wat-for-reals:GEO1
- U$181: device Labels:GND-04 -> wt_dir:D#0
- U$182: device Labels:MISO-(]-04 -> wt_dir:D#1
- U$183: device Labels:MOSI-(]-04 -> wt_dir:W#2
- U$184: device wt_dir:D#0 -> wt_dir:W#3
- U$185: device wt_dir:D#1 -> SparkFun-Aesthetics:SFE_LOGO_FLAME_.2
- U$186: device wt_dir:W#2 -> Labels:SCL-[)
- U$187: device wt_dir:W#3 -> Labels:SDA-[)
- U$188: device Labels:5V -> Labels:3V3-04
- U$189: device ALL_LABELS:INT1 -> Labels:GND-04
- U$190: device ALL_LABELS:PPS4 -> Labels:3V3-04
- U$192: device moar:TXO21 -> Labels:MISO-(]-04
- U$193: device txr_rxi:RXI22 -> Labels:MOSI-(]-04
- U$194: device txr_rxi:SCLK1 -> wt_dir:D#0
- U$195: device txr_rxi:TXR0 -> wt_dir:D#1
- U$196: device dead reckoning:GPS_DEAD_RECKONING0 -> wt_dir:W#2
- U$197: device Dead#Reckoning#GPS#board#silk#FINAL#png:DEAD#RECKONING#GPS#BOARD#SILK#FINAL#JPG -> wt_dir:W#3
- U$198: device Dead#Reckoning#GPS#board#silk#FINALSMALL:DEAD#RECKONING#GPS#BOARD#SILK#FINAL#JPG -> Labels:5V
- U$199: device Labels:CS#-<]-04 -> ALL_LABELS:INT1
- U$200: device ALL labels:PPS8 -> ALL_LABELS:PPS4
- U$201: device ALL labels:PWR10 -> Labels:GND-04
- U$202: device ALL labels:RTK9 -> moar:TXO21
- U$203: device TXR:BLK2 -> txr_rxi:RXI22
- U$204: device TXR:GRN1 -> txr_rxi:SCLK1
- U$205: device Labels:3V3-04 -> txr_rxi:TXR0
- U$206: device Labels:GND-04 -> dead reckoning:GPS_DEAD_RECKONING0
- U$207: device Labels:3V3-04 -> Dead#Reckoning#GPS#board#silk#FINAL#png:DEAD#RECKONING#GPS#BOARD#SILK#FINAL#JPG
- U$208: device Labels:GND-04 -> Dead#Reckoning#GPS#board#silk#FINALSMALL:DEAD#RECKONING#GPS#BOARD#SILK#FINAL#JPG
- U$209: device Labels:5V -> Orientation:X1
- U$211: device ALL_LABELS:RXI28 -> Orientation:Y2
- U$212: device moar:TXO21 -> Orientation:Z0
- U$213: device more_all_labels:SPI4 -> Orientation:Z0
- U$214: device Labels:I_SUPER2_C-()-04 -> Labels:CS#-<]-04
- U$215: device ALL labels:RTK9 -> ALL labels:PPS8
- U$216: device ALL labels:PPS8 -> ALL labels:PWR10
- U$217: device ALL labels:PWR10 -> ALL labels:RTK9
- U$218: device ant:ANT0 -> TXR:BLK2
- U$219: device zed:ZED#F9R0 -> TXR:GRN1
- U$220: device TXR:GRN1 -> Labels:3V3-04
- U$221: device TXR:BLK2 -> Labels:GND-04
- U$222: device bottom labels:INT2 -> Labels:3V3-04
- U$223: device bottom labels:PPS1 -> Labels:GND-04
- U$224: device Labels:CS#-[>-04 -> Labels:5V
- U$225: device corrected_bottom:RXI#MOSI0 -> Labels:GND-04
- U$226: device corrected_bottom:TXO#MISO1 -> ALL_LABELS:RXI28
- U$227: device corrected_bottom:SCL#CLK2 -> moar:TXO21
- U$228: device corrected_bottom:SCL5 -> more_all_labels:SPI4
- U$229: device corrected_bottom:SDA4 -> Labels:I_SUPER2_C-()-04
- U$230: device corrected_bottom:TXR3 -> ALL labels:RTK9
- U$231: device corrected_safe_reset:#RESET1 -> ALL labels:PPS8
- U$232: device corrected_safe_reset:#RESET2 -> ALL labels:PWR10
- U$233: device corrected_safe_reset:#SAFEBOOT3 -> ant:ANT0
- U$234: device wat-for-reals:#SFBT0 -> zed:ZED#F9R0
- U$235: device wat-for-reals:GEO1 -> TXR:GRN1
- U$236: device wat-for-reals:GEO1 -> TXR:BLK2
- U$237: device wt_dir:D#0 -> bottom labels:INT2
- U$238: device wt_dir:D#1 -> bottom labels:PPS1
- U$239: device wt_dir:W#2 -> Labels:CS#-[>-04
- U$240: device wt_dir:W#3 -> corrected_bottom:RXI#MOSI0
- U$241: device SparkFun-Aesthetics:SFE_LOGO_FLAME_.2 -> corrected_bottom:TXO#MISO1
- U$242: device Labels:SCL-[) -> corrected_bottom:SCL#CLK2
- U$243: device Labels:SDA-[) -> corrected_bottom:SCL5
- U$244: device Labels:3V3-04 -> corrected_bottom:SDA4
- U$245: device Labels:GND-04 -> corrected_bottom:TXR3
- U$246: device Labels:3V3-04 -> corrected_safe_reset:#RESET1
- U$247: device Labels:GND-04 -> corrected_safe_reset:#RESET2
- U$248: device Labels:MISO-(]-04 -> corrected_safe_reset:#SAFEBOOT3
- U$249: device Labels:MOSI-(]-04 -> wat-for-reals:#SFBT0
- U$250: device wt_dir:D#0 -> wat-for-reals:GEO1
- U$251: device wt_dir:D#1 -> wat-for-reals:GEO1
- U$252: device wt_dir:W#2 -> wt_dir:D#0
- U$253: device wt_dir:W#3 -> wt_dir:D#1
- U$254: device Labels:5V -> wt_dir:W#2
- U$255: device ALL_LABELS:INT1 -> wt_dir:W#3
- U$256: device ALL_LABELS:PPS4 -> SparkFun-Aesthetics:SFE_LOGO_FLAME_.2
- U$258: device moar:TXO21 -> Labels:SDA-[)
- U$259: device txr_rxi:RXI22 -> Labels:3V3-04
- U$260: device txr_rxi:SCLK1 -> Labels:GND-04
- U$261: device txr_rxi:TXR0 -> Labels:3V3-04
- U$263: device Dead#Reckoning#GPS#board#silk#FINAL#png:DEAD#RECKONING#GPS#BOARD#SILK#FINAL#JPG -> Labels:MISO-(]-04
- U$264: device Dead#Reckoning#GPS#board#silk#FINALSMALL:DEAD#RECKONING#GPS#BOARD#SILK#FINAL#JPG -> Labels:MOSI-(]-04
- U$32: device Labels:CS#-<]-04 -> Orientation:X1
- U$50: device ALL labels:PPS8 -> Orientation:Y2
- U$52: device ALL labels:PWR10 -> Orientation:Y2
- U$57: device ALL labels:RTK9 -> Orientation:Z0
- U$63: device TXR:BLK2 -> Orientation:Z0
- U$72: device TXR:GRN1 -> Labels:CS#-<]-04
- U$73: device Labels:3V3-04 -> ALL labels:PPS8
- U$74: device Labels:GND-04 -> ALL labels:PWR10
- U$75: device Labels:3V3-04 -> ALL labels:RTK9
- U$76: device Labels:GND-04 -> TXR:BLK2
- U$77: device Labels:5V -> TXR:GRN1
- U$78: device Labels:GND-04 -> Labels:3V3-04
- U$79: device ALL_LABELS:RXI28 -> Labels:GND-04
- U$80: device moar:TXO21 -> Labels:3V3-04
- U$81: device more_all_labels:SPI4 -> Labels:GND-04
- U$82: device Labels:I_SUPER2_C-()-04 -> Labels:5V
- U$83: device ALL labels:RTK9 -> Labels:GND-04
- U$84: device ALL labels:PPS8 -> ALL_LABELS:RXI28
- U$85: device ALL labels:PWR10 -> moar:TXO21
- U$86: device ant:ANT0 -> more_all_labels:SPI4
- U$87: device zed:ZED#F9R0 -> Labels:I_SUPER2_C-()-04
- U$88: device TXR:GRN1 -> ALL labels:RTK9
- U$89: device TXR:BLK2 -> ALL labels:PPS8
- U$90: device bottom labels:INT2 -> ALL labels:PWR10
- U$91: device bottom labels:PPS1 -> ant:ANT0
- U$92: device Labels:CS#-[>-04 -> zed:ZED#F9R0
- U$93: device corrected_bottom:RXI#MOSI0 -> TXR:GRN1
- U$94: device corrected_bottom:TXO#MISO1 -> TXR:BLK2
- U$95: device corrected_bottom:SCL#CLK2 -> bottom labels:INT2
- U$96: device corrected_bottom:SCL5 -> bottom labels:PPS1
- U$97: device corrected_bottom:SDA4 -> Labels:CS#-[>-04
- U$98: device corrected_bottom:TXR3 -> corrected_bottom:RXI#MOSI0
- U$99: device corrected_safe_reset:#RESET1 -> corrected_bottom:TXO#MISO1
- moved U$137 102.0 mm to (60.7, 4.70)
- moved U$138 97.0 mm to (49.9, 12.1)
- moved U$140 90.4 mm to (56.6, 15.5)
- moved U$139 86.8 mm to (53.8, 15.5), flipped to the top
- moved U$209 82.2 mm to (6.22, 65.9), flipped to the top
- moved U$199 80.9 mm to (1.57, 72.9)
- moved U$63 78.8 mm to (8.38, 13.5)
- moved U$142 77.9 mm to (52.1, 13.5), flipped to the top
- moved U$32 77.5 mm to (6.22, 12.1)
- moved U$208 75.4 mm to (17.0, 58.5), flipped to the top
- moved U$133 74.4 mm to (80.0, 21.6)
- moved U$210 73.7 mm to (10.2, 69.3), flipped to the top, turned to 0 degrees
- moved U$141 73.3 mm to (54.9, 13.5)
- moved U$200 69.8 mm to (1.68, 70.3)
- moved U$57 67.5 mm to (11.2, 13.5), flipped to the bottom
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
